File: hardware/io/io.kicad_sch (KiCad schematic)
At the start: 784 parts, among them J1 USB_B, J10 Conn_02x18_Odd_Even, J11 Barrel_Jack_Switch_Pin3Ring, J2 Conn_02x03_Odd_Even, J3 Conn_02x08_Odd_Even, J4 Conn_02x40_Odd_Even, J5 Conn_02x16_Odd_Even, J6 Conn_02x16_Odd_Even, J7 Conn_02x12_Odd_Even, J8 Conn_02x24_Odd_Even, Q129 IRLML6244, Q130 IRLML6402, Q131 IRLML6244, Q132 IRLML6402, Q133 IRLML6244, Q134 IRLML6402, Q135 IRLML6244, Q136 IRLML6402, Q137 IRLML6244, Q138 IRLML6402, Q139 IRLML6244, Q140 IRLML6402, Q141 IRLML6244, Q142 IRLML6402, Q143 IRLML6244, Q144 IRLML6402, Q145 IRLML6244, Q146 IRLML6402, Q147 IRLML6244, Q148 IRLML6402, Q149 IRLML6244, Q150 IRLML6402, Q151 IRLML6244, Q152 IRLML6402, Q153 IRLML6244, Q154 IRLML6402, Q155 IRLML6244, Q156 IRLML6402, Q157 IRLML6244, Q158 IRLML6402, Q159 IRLML6244, Q160 IRLML6402, Q161 IRLML6244, Q162 IRLML6402, Q163 IRLML6244, Q164 IRLML6402, Q165 IRLML6244, Q166 IRLML6402, Q167 IRLML6244, Q168 IRLML6402, Q169 IRLML6244, Q170 IRLML6402, Q171 IRLML6244, Q172 IRLML6402, Q173 IRLML6244, Q174 IRLML6402, Q175 IRLML6244, Q176 IRLML6402, Q177 IRLML6244, Q178 IRLML6402, Q179 IRLML6244, Q180 IRLML6402, Q181 IRLML6244, Q182 IRLML6402, Q183 IRLML6244, Q184 IRLML6402, Q185 IRLML6244, Q186 IRLML6402, Q187 IRLML6244, Q188 IRLML6402, Q189 IRLML6244, Q190 IRLML6402, Q191 IRLML6244, Q192 IRLML6402, Q193 IRLML6244, Q194 IRLML6402, Q195 IRLML6244, Q196 IRLML6402, Q197 IRLML6244, Q198 IRLML6402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

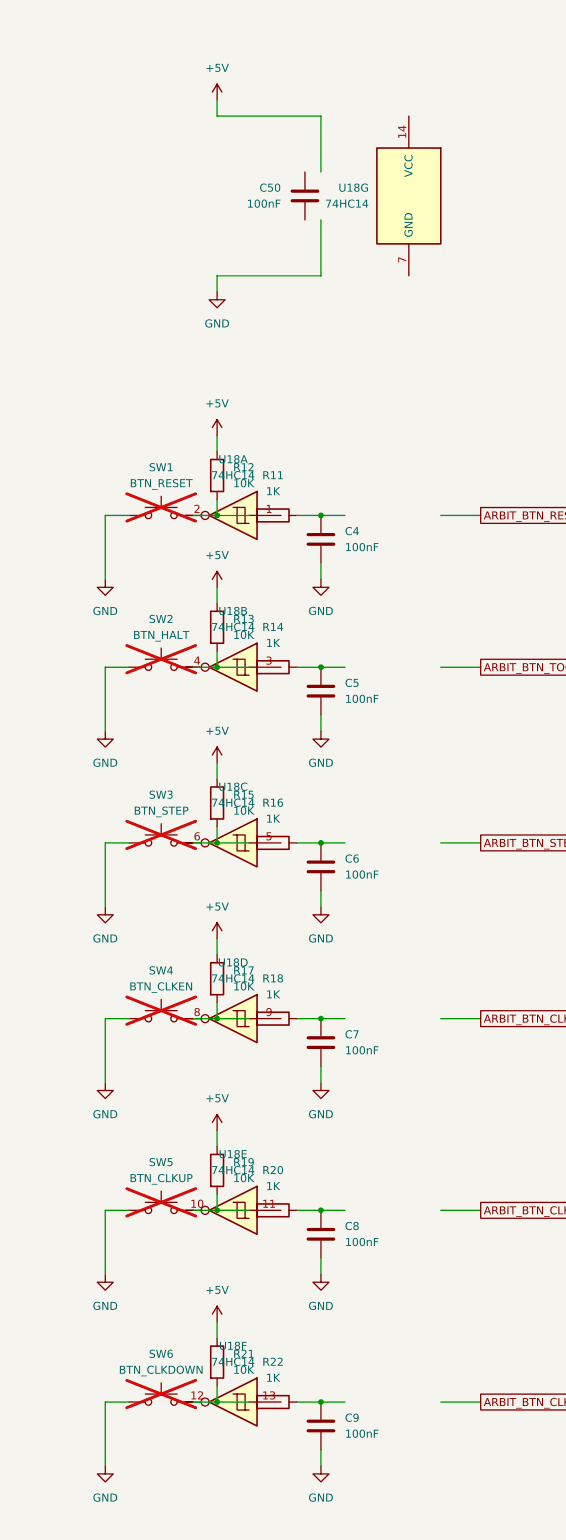
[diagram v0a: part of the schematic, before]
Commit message: more work on IO PCB routing
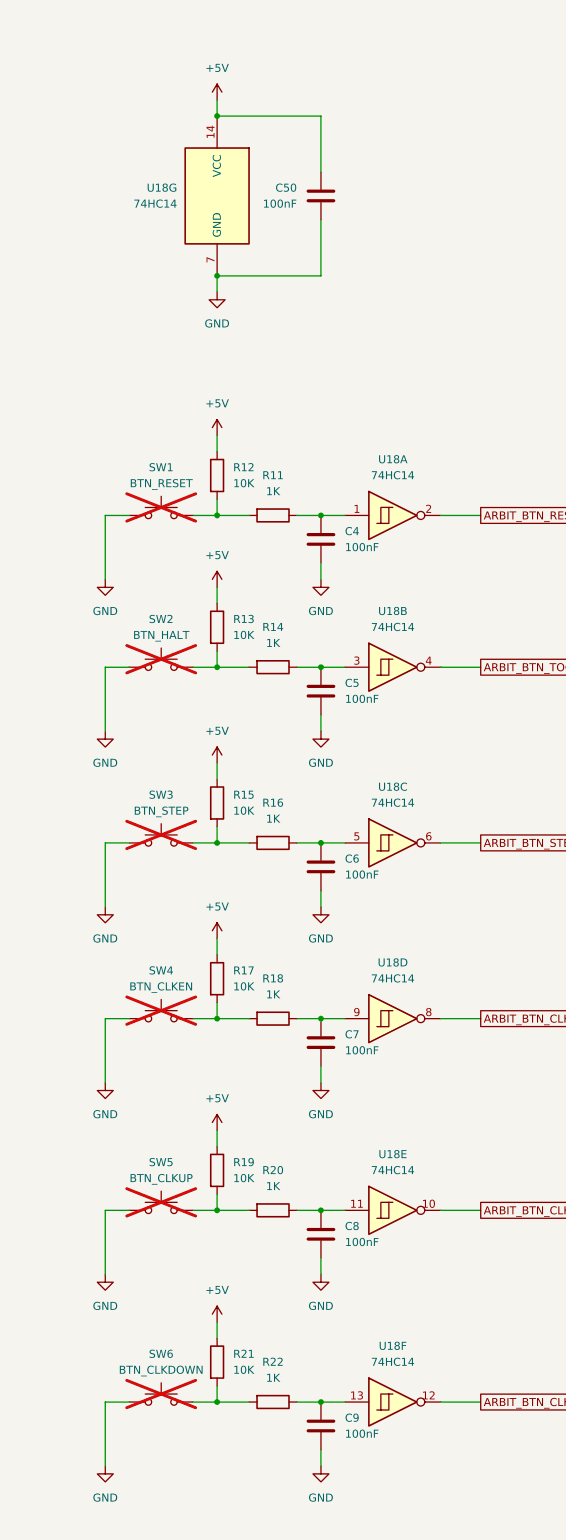
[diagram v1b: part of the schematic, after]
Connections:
- net +5V: now also C50.2, U18.14 (VCC)
- net ARBIT_BTN_CLKDOWN: now also U18.12
- net ARBIT_BTN_CLKEN: now also U18.8
- net ARBIT_BTN_CLKUP: now also U18.10
- net ARBIT_BTN_RESET: now also U18.2
- net ARBIT_BTN_STEP: now also U18.6
- net ARBIT_BTN_TOGGLEHALT: now also U18.4
- net GND: now also C50.1, U18.7 (GND)
- net at C8.2, R20.1: now also U18.11
- net at C6.2, R16.1: now also U18.5
- net at C4.2, R11.1: now also U18.1
- net at U18.9: now also C7.2, R18.1
- net at C5.2, R14.1: now also U18.3
- net at C9.2, R22.1: now also U18.13
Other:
- moved on the sheet: C50, U18A, U18B, U18C, U18D, U18E, U18F, U18G
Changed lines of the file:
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@@
 	)
 	(junction
+		(at 97.79 543.56)
+		(diameter 0)
+		(color 0 0 0 0)
+	)
+	(junction
 		(at 1629.41 805.18)
 		(diameter 0)
@@
 	)
 	(junction
+		(at 97.79 518.16)
+		(diameter 0)
+		(color 0 0 0 0)
+	)
+	(junction
 		(at 1360.17 499.11)
 		(diameter 0)
@@
 	(symbol
 		(lib_id "74xx:74HC14")
-		(at 100.33 633.73 0)
-		(mirror y)
+		(at 125.73 633.73 0)
 		(unit 3)
 		(exclude_from_sim no)
@@
 		(on_board yes)
 		(dnp no)
-		(fields_autoplaced yes)
 		(property "Reference" "U18"
-			(at 100.33 624.84 0)
+			(at 125.73 624.84 0)
 			(effects
 				(font
@@
 		)
 		(property "Value" "74HC14"
-			(at 100.33 627.38 0)
+			(at 125.73 627.38 0)
 			(effects
 				(font
@@
 		)
 		(property "Footprint" "Package_SO:SOIC-14_3.9x8.7mm_P1.27mm"
-			(at 100.33 633.73 0)
+			(at 125.73 633.73 0)
 			(effects
 				(font
@@
 		)
 		(property "Datasheet" "http://www.ti.com/lit/gpn/sn74HC14"
-			(at 100.33 633.73 0)
+			(at 125.73 633.73 0)
 			(effects
 				(font
@@
 		)
 		(property "Description" "Hex inverter schmitt trigger"
-			(at 100.33 633.73 0)
+			(at 125.73 633.73 0)
 			(effects
 				(font
@@
 	(symbol
 		(lib_id "Device:C")
-		(at 111.76 530.86 0)
+		(at 114.3 530.86 0)
 		(mirror x)
 		(unit 1)
@@
 		(fields_autoplaced yes)
 		(property "Reference" "C50"
-			(at 107.95 529.5899 0)
+			(at 110.49 529.5899 0)
 			(effects
 				(font
@@
 		)
 		(property "Value" "100nF"
-			(at 107.95 532.1299 0)
+			(at 110.49 532.1299 0)
 			(effects
 				(font
@@
 		)
 		(property "Footprint" "Capacitor_SMD:C_0402_1005Metric"
-			(at 112.7252 527.05 0)
+			(at 115.2652 527.05 0)
 			(effects
 				(font
@@
 		)
 		(property "Datasheet" "~"
-			(at 111.76 530.86 0)
+			(at 114.3 530.86 0)
 			(effects
 				(font
@@
 		)
 		(property "Description" "Unpolarized capacitor"
-			(at 111.76 530.86 0)
+			(at 114.3 530.86 0)
 			(effects
 				(font
@@
 	(symbol
 		(lib_id "74xx:74HC14")
-		(at 100.33 661.67 0)
-		(mirror y)
+		(at 125.73 661.67 0)
 		(unit 4)
 		(exclude_from_sim no)
@@
 		(on_board yes)
 		(dnp no)
-		(fields_autoplaced yes)
 		(property "Reference" "U18"
-			(at 100.33 652.78 0)
+			(at 125.73 652.78 0)
 			(effects
 				(font
@@
 		)
 		(property "Value" "74HC14"
-			(at 100.33 655.32 0)
+			(at 125.73 655.32 0)
 			(effects
 				(font
@@
 		)
 		(property "Footprint" "Package_SO:SOIC-14_3.9x8.7mm_P1.27mm"
-			(at 100.33 661.67 0)
+			(at 125.73 661.67 0)
 			(effects
 				(font
@@
 		)
 		(property "Datasheet" "http://www.ti.com/lit/gpn/sn74HC14"
-			(at 100.33 661.67 0)
+			(at 125.73 661.67 0)
 			(effects
 				(font
@@
 		)
 		(property "Description" "Hex inverter schmitt trigger"
-			(at 100.33 661.67 0)
+			(at 125.73 661.67 0)
 			(effects
 				(font
@@
 	(symbol
 		(lib_id "74xx:74HC14")
-		(at 100.33 692.15 0)
-		(mirror y)
+		(at 125.73 692.15 0)
 		(unit 5)
 		(exclude_from_sim no)
@@
 		(on_board yes)
 		(dnp no)
-		(fields_autoplaced yes)
 		(property "Reference" "U18"
-			(at 100.33 683.26 0)
+			(at 125.73 683.26 0)
 			(effects
 				(font
@@
 		)
 		(property "Value" "74HC14"
-			(at 100.33 685.8 0)
+			(at 125.73 685.8 0)
 			(effects
 				(font
@@
 		)
 		(property "Footprint" "Package_SO:SOIC-14_3.9x8.7mm_P1.27mm"
-			(at 100.33 692.15 0)
+			(at 125.73 692.15 0)
 			(effects
 				(font
@@
 		)
 		(property "Datasheet" "http://www.ti.com/lit/gpn/sn74HC14"
-			(at 100.33 692.15 0)
+			(at 125.73 692.15 0)
 			(effects
 				(font
@@
 		)
 		(property "Description" "Hex inverter schmitt trigger"
-			(at 100.33 692.15 0)
+			(at 125.73 692.15 0)
 			(effects
 				(font
@@
 	(symbol
 		(lib_id "74xx:74HC14")
-		(at 100.33 581.66 0)
-		(mirror y)
+		(at 125.73 581.66 0)
 		(unit 1)
 		(exclude_from_sim no)
@@
 		(on_board yes)
 		(dnp no)
-		(fields_autoplaced yes)
 		(property "Reference" "U18"
-			(at 100.33 572.77 0)
+			(at 125.73 572.77 0)
 			(effects
 				(font
@@
 		)
 		(property "Value" "74HC14"
-			(at 100.33 575.31 0)
+			(at 125.73 575.31 0)
 			(effects
 				(font
@@
 		)
 		(property "Footprint" "Package_SO:SOIC-14_3.9x8.7mm_P1.27mm"
-			(at 100.33 581.66 0)
+			(at 125.73 581.66 0)
 			(effects
 				(font
@@
 		)
 		(property "Datasheet" "http://www.ti.com/lit/gpn/sn74HC14"
-			(at 100.33 581.66 0)
+			(at 125.73 581.66 0)
 			(effects
 				(font
@@
 		)
 		(property "Description" "Hex inverter schmitt trigger"
-			(at 100.33 581.66 0)
+			(at 125.73 581.66 0)
 			(effects
 				(font
@@
 	(symbol
 		(lib_id "74xx:74HC14")
-		(at 128.27 530.86 0)
+		(at 97.79 530.86 0)
 		(mirror y)
 		(unit 7)
@@
 		(fields_autoplaced yes)
 		(property "Reference" "U18"
-			(at 121.92 529.5899 0)
+			(at 91.44 529.5899 0)
 			(effects
 				(font
@@
 		)
 		(property "Value" "74HC14"
-			(at 121.92 532.1299 0)
+			(at 91.44 532.1299 0)
 			(effects
 				(font
@@
 		)
 		(property "Footprint" "Package_SO:SOIC-14_3.9x8.7mm_P1.27mm"
-			(at 128.27 530.86 0)
+			(at 97.79 530.86 0)
 			(effects
 				(font
@@
 		)
 		(property "Datasheet" "http://www.ti.com/lit/gpn/sn74HC14"
-			(at 128.27 530.86 0)
+			(at 97.79 530.86 0)
 			(effects
 				(font
@@
 		)
 		(property "Description" "Hex inverter schmitt trigger"
-			(at 128.27 530.86 0)
+			(at 97.79 530.86 0)
 			(effects
 				(font
@@
 	(symbol
 		(lib_id "74xx:74HC14")
-		(at 100.33 605.79 0)
-		(mirror y)
+		(at 125.73 605.79 0)
 		(unit 2)
 		(exclude_from_sim no)
@@
 		(on_board yes)
 		(dnp no)
-		(fields_autoplaced yes)
 		(property "Reference" "U18"
-			(at 100.33 596.9 0)
+			(at 125.73 596.9 0)
 			(effects
 				(font
@@
 		)
 		(property "Value" "74HC14"
-			(at 100.33 599.44 0)
+			(at 125.73 599.44 0)
 			(effects
 				(font
@@
 		)
 		(property "Footprint" "Package_SO:SOIC-14_3.9x8.7mm_P1.27mm"
-			(at 100.33 605.79 0)
+			(at 125.73 605.79 0)
 			(effects
 				(font
@@
 		)
 		(property "Datasheet" "http://www.ti.com/lit/gpn/sn74HC14"
-			(at 100.33 605.79 0)
+			(at 125.73 605.79 0)
 			(effects
 				(font
@@
 		)
 		(property "Description" "Hex inverter schmitt trigger"
-			(at 100.33 605.79 0)
+			(at 125.73 605.79 0)
 			(effects
 				(font
@@
 	(symbol
 		(lib_id "74xx:74HC14")
-		(at 100.33 722.63 0)
-		(mirror y)
+		(at 125.73 722.63 0)
 		(unit 6)
 		(exclude_from_sim no)
@@
 		(on_board yes)
 		(dnp no)
-		(fields_autoplaced yes)
 		(property "Reference" "U18"
-			(at 100.33 713.74 0)
+			(at 125.73 713.74 0)
 			(effects
 				(font
@@
 		)
 		(property "Value" "74HC14"
-			(at 100.33 716.28 0)
+			(at 125.73 716.28 0)
 			(effects
 				(font
@@
 		)
 		(property "Footprint" "Package_SO:SOIC-14_3.9x8.7mm_P1.27mm"
-			(at 100.33 722.63 0)
+			(at 125.73 722.63 0)
 			(effects
 				(font
@@
 		)
 		(property "Datasheet" "http://www.ti.com/lit/gpn/sn74HC14"
-			(at 100.33 722.63 0)
+			(at 125.73 722.63 0)
 			(effects
 				(font
@@
 		)
 		(property "Description" "Hex inverter schmitt trigger"
-			(at 100.33 722.63 0)
+			(at 125.73 722.63 0)
 			(effects
 				(font

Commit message: io pcb done. :)
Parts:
- added H1, H2, H3, H4, H5, H6, H7, H8: MountingHole_Pad, MountingHole:MountingHole_3.2mm_M3_ISO7380_Pad_TopBottom, symbol Mechanical:MountingHole_Pad
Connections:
- net GND: now also H1.1, H2.1, H3.1, H4.1, H5.1, H6.1, H7.1, H8.1

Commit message: added Traco DCDC, not hooked up yet
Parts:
- added U93: TSR3-2450N, Converter_DCDC:Converter_DCDC_TRACO_TSR2-24xxN_TSR2-24xxxN_THT, symbol Regulator_Switching:TSR3-2450N
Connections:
- net +5V: now also U93.3 (Vout); no longer D6.1 (K), Q2.3 (S)
- net GND: now also U93.2 (GND)
- new net: D6.1 (K), Q2.3 (S), U93.1 (Vin)
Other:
- moved on the sheet: C26, C41, C97, C98, J11, R24, R25, R26, R27, R28, R29, R30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
